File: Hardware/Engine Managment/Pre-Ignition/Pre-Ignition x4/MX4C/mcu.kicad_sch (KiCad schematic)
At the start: 4 parts, among them J8 Reset Control

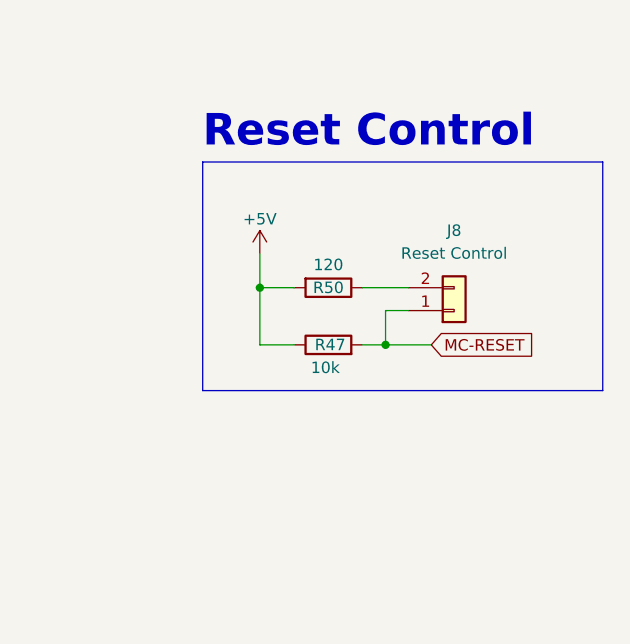
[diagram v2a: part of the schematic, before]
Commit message: minor update
Copper Pour and clearances updated.
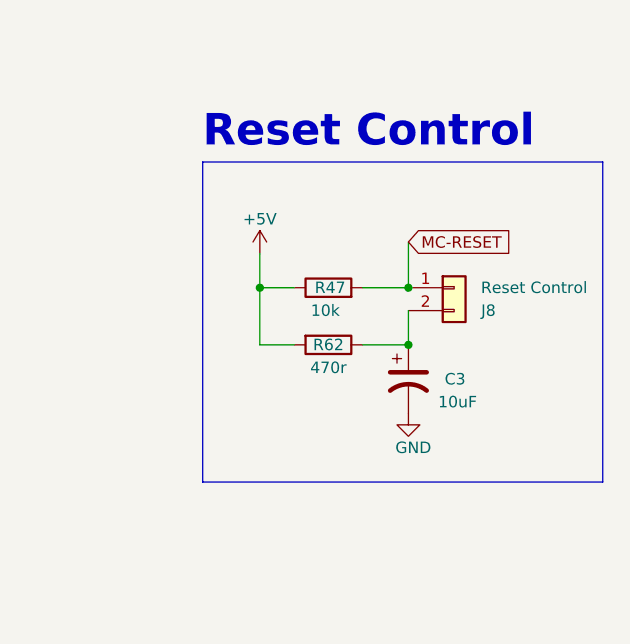
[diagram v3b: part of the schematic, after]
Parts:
- removed R50: 120, Resistor_SMD:R_0402_1005Metric, symbol Device:R
- added C3: 10uF, Capacitor_Tantalum_SMD:CP_EIA-3216-18_Kemet-A, symbol Device:C_Polarized_US
- added R62: 470r, Resistor_SMD:R_0402_1005Metric, symbol Device:R
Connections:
- net +5V: now also R62.2
- net GND: now also C3.2
- net at J8.2 (Pin_2): now also C3.1, R62.1
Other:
- moved on the sheet: R47
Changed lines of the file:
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@@
   (title_block
     (title "Pre-Ignition X4")
-    (date "2023-06-15")
+    (date "2023-10-24")
     (rev "C")
     (company "DetonationEMS")
@@
   (junction (at 57.15 128.27) (diameter 0) (color 0 0 0 0)
   )
+  (junction (at 190.5 115.57) (diameter 0) (color 0 0 0 0)
+  )
   (junction (at 173.99 109.22) (diameter 0) (color 0 0 0 0)
   )
   (junction (at 57.15 133.35) (diameter 0) (color 0 0 0 0)
   )
-  (junction (at 187.96 115.57) (diameter 0) (color 0 0 0 0)
+  (junction (at 190.5 109.22) (diameter 0) (color 0 0 0 0)
   )
   (wire (pts (xy 40.64 146.05) (xy 57.15 146.05))
@@
     (stroke (width 0) (type default))
   )
-  (wire (pts (xy 187.96 111.76) (xy 187.96 115.57))
+  (wire (pts (xy 190.5 111.76) (xy 190.5 115.57))
     (stroke (width 0) (type default))
   )
@@
     (stroke (width 0) (type default))
   )
-  (wire (pts (xy 187.96 115.57) (xy 193.04 115.57))
+  (wire (pts (xy 190.5 104.14) (xy 190.5 109.22))
     (stroke (width 0) (type default))
   )
@@
     (stroke (width 0) (type default))
   )
-  (polyline (pts (xy 167.64 120.65) (xy 212.09 120.65))
+  (polyline (pts (xy 167.64 130.81) (xy 212.09 130.81))
     (stroke (width 0) (type default))
   )
@@
     (stroke (width 0) (type default))
   )
+  (wire (pts (xy 185.42 115.57) (xy 190.5 115.57))
+    (stroke (width 0) (type default))
+  )
   (wire (pts (xy 57.15 128.27) (xy 57.15 130.81))
     (stroke (width 0) (type default))
@@
     (stroke (width 0) (type default))
   )
-  (polyline (pts (xy 212.09 120.65) (xy 212.09 95.25))
+  (polyline (pts (xy 212.09 130.81) (xy 212.09 95.25))
     (stroke (width 0) (type default))
   )
@@
     (stroke (width 0) (type default))
   )
-  (wire (pts (xy 190.5 111.76) (xy 187.96 111.76))
-    (stroke (width 0) (type default))
-  )
   (wire (pts (xy 45.72 140.97) (xy 64.77 140.97))
     (stroke (width 0) (type default))
   )
-  (polyline (pts (xy 167.64 95.25) (xy 167.64 120.65))
+  (polyline (pts (xy 167.64 95.25) (xy 167.64 130.81))
     (stroke (width 0) (type default))
   )
@@
   )
   (wire (pts (xy 60.96 100.33) (xy 64.77 100.33))
-    (stroke (width 0) (type default))
-  )
-  (wire (pts (xy 185.42 115.57) (xy 187.96 115.57))
     (stroke (width 0) (type default))
   )
@@
     )
   )
-  (global_label "MC-RESET" (shape input) (at 193.04 115.57 0) (fields_autoplaced)
-    (effects (font (size 1.27 1.27)) (justify left))
-    (property "Intersheetrefs" "${INTERSHEET_REFS}" (at 101.6 -19.05 0)
+  (global_label "MC-RESET" (shape input) (at 190.5 104.14 0) (fields_autoplaced)
+    (effects (font (size 1.27 1.27)) (justify left))
+    (property "Intersheetrefs" "${INTERSHEET_REFS}" (at 99.06 -30.48 0)
       (effects (font (size 1.27 1.27)) hide)
     )
@@
     )
   )
-  (symbol (lib_id "Device:R") (at 181.61 115.57 90) (unit 1)
+  (symbol (lib_id "Device:R") (at 181.61 109.22 90) (unit 1)
     (in_bom yes) (on_board yes) (dnp no)
-    (property "Reference" "R47" (at 183.515 115.57 90)
+    (property "Reference" "R47" (at 183.515 109.22 90)
       (effects (font (size 1.27 1.27)) (justify left))
     )
-    (property "Value" "10k" (at 182.88 118.11 90)
+    (property "Value" "10k" (at 182.88 111.76 90)
       (effects (font (size 1.27 1.27)) (justify left))
     )
-    (property "Footprint" "Resistor_SMD:R_0603_1608Metric" (at 181.61 117.348 90)
-      (effects (font (size 1.27 1.27)) hide)
-    )
-    (property "Datasheet" "~" (at 181.61 115.57 0)
-      (effects (font (size 1.27 1.27)) hide)
-    )
-    (property "LCSC" "C25804" (at 181.61 115.57 0)
+    (property "Footprint" "Resistor_SMD:R_0603_1608Metric" (at 181.61 110.998 90)
+      (effects (font (size 1.27 1.27)) hide)
+    )
+    (property "Datasheet" "~" (at 181.61 109.22 0)
+      (effects (font (size 1.27 1.27)) hide)
+    )
+    (property "LCSC" "C25804" (at 181.61 109.22 0)
       (effects (font (size 1.27 1.27)) hide)
     )
@@
     )
   )
+  (symbol (lib_id "Device:R") (at 181.61 115.57 270) (unit 1)
+    (in_bom yes) (on_board yes) (dnp no)
+    (property "Reference" "R62" (at 181.61 115.57 90)
+      (effects (font (size 1.27 1.27)))
+    )
+    (property "Value" "470r" (at 181.61 118.11 90)
+      (effects (font (size 1.27 1.27)))
+    )
+    (property "Footprint" "Resistor_SMD:R_0402_1005Metric" (at 181.61 113.792 90)
+      (effects (font (size 1.27 1.27)) hide)
+    )
+    (property "Datasheet" "~" (at 181.61 115.57 0)
+      (effects (font (size 1.27 1.27)) hide)
+    )
+    (property "LCSC" "C25117" (at 181.61 115.57 0)
+      (effects (font (size 1.27 1.27)) hide)
+    )
+    (pin "1")
+    (pin "2")
+    (instances
+      (project "Pre_Ignition"
+        (path "/929a9b03-e99e-4b88-8e16-759f8c6b59a5/00000000-0000-0000-0000-000060e7aa2a"
+          (reference "R62") (unit 1)
+        )
+        (path "/929a9b03-e99e-4b88-8e16-759f8c6b59a5/651424fd-2282-475b-821e-32691fc06f26"
+          (reference "R62") (unit 1)
+        )
+      )
+    )
+  )
   (symbol (lib_id "power:GND") (at 53.34 128.27 0) (unit 1)
     (in_bom yes) (on_board yes) (dnp no)
@@
     )
   )
-  (symbol (lib_id "Connector_Generic:Conn_01x02") (at 195.58 111.76 0) (mirror x) (unit 1)
-    (in_bom yes) (on_board yes) (dnp no) (fields_autoplaced)
-    (property "Reference" "J8" (at 195.58 102.87 0)
+  (symbol (lib_id "Connector_Generic:Conn_01x02") (at 195.58 109.22 0) (unit 1)
+    (in_bom yes) (on_board yes) (dnp no)
+    (property "Reference" "J8" (at 199.39 111.76 0)
       (effects (font (size 1.27 1.27)))
     )
-    (property "Value" "Reset Control" (at 195.58 105.41 0)
+    (property "Value" "Reset Control" (at 204.47 109.22 0)
       (effects (font (size 1.27 1.27)))
     )
-    (property "Footprint" "Detonation:1x02-Proto" (at 195.58 111.76 0)
-      (effects (font (size 1.27 1.27)) hide)
-    )
-    (property "Datasheet" "~" (at 195.58 111.76 0)
+    (property "Footprint" "Detonation:1x02-Proto" (at 195.58 109.22 0)
+      (effects (font (size 1.27 1.27)) hide)
+    )
+    (property "Datasheet" "~" (at 195.58 109.22 0)
       (effects (font (size 1.27 1.27)) hide)
     )
@@
     )
   )
-  (symbol (lib_id "Device:R") (at 181.61 109.22 270) (unit 1)
+  (symbol (lib_id "Device:C_Polarized_US") (at 190.5 119.38 0) (unit 1)
     (in_bom yes) (on_board yes) (dnp no)
-    (property "Reference" "R50" (at 181.61 109.22 90)
-      (effects (font (size 1.27 1.27)))
-    )
-    (property "Value" "120" (at 181.61 106.68 90)
-      (effects (font (size 1.27 1.27)))
-    )
-    (property "Footprint" "Resistor_SMD:R_0402_1005Metric" (at 181.61 107.442 90)
-      (effects (font (size 1.27 1.27)) hide)
-    )
-    (property "Datasheet" "~" (at 181.61 109.22 0)
-      (effects (font (size 1.27 1.27)) hide)
-    )
-    (property "LCSC" "C25079" (at 181.61 109.22 0)
+    (property "Reference" "C3" (at 196.85 119.38 0)
+      (effects (font (size 1.27 1.27)) (justify right))
+    )
+    (property "Value" "10uF" (at 198.12 121.92 0)
+      (effects (font (size 1.27 1.27)) (justify right))
+    )
+    (property "Footprint" "Capacitor_Tantalum_SMD:CP_EIA-3216-18_Kemet-A" (at 190.5 119.38 0)
+      (effects (font (size 1.27 1.27)) hide)
+    )
+    (property "Datasheet" "~" (at 190.5 119.38 0)
+      (effects (font (size 1.27 1.27)) hide)
+    )
+    (property "LCSC" "C7171" (at 190.5 119.38 0)
+      (effects (font (size 1.27 1.27)) hide)
+    )
+    (property "Manufacture Part Number" "TAJA106K016RNJ" (at 190.5 119.38 0)
       (effects (font (size 1.27 1.27)) hide)
     )
@@
     (instances
       (project "Pre_Ignition"
+        (path "/4af6cfdf-466c-4a30-a9ae-01184b002ed6/46f448a6-75c3-4ecc-b10a-dcee0521adb1"
+          (reference "C3") (unit 1)
+        )
+      )
+      (project "Pre_Ignition"
+        (path "/929a9b03-e99e-4b88-8e16-759f8c6b59a5/fd679192-a7db-468f-89ad-a9c384ea113f"
+          (reference "C33") (unit 1)
+        )
         (path "/929a9b03-e99e-4b88-8e16-759f8c6b59a5/651424fd-2282-475b-821e-32691fc06f26"
-          (reference "R50") (unit 1)
+          (reference "C31") (unit 1)
         )
       )
@@
         )
       )
+    )
+  )
+  (symbol (lib_id "power:GND") (at 190.5 123.19 0) (unit 1)
+    (in_bom yes) (on_board yes) (dnp no)
+    (property "Reference" "#PWR051" (at 190.5 129.54 0)
+      (effects (font (size 1.27 1.27)) hide)
+    )
+    (property "Value" "GND" (at 193.04 127 0)
+      (effects (font (size 1.27 1.27)) (justify right))
+    )
+    (property "Footprint" "" (at 190.5 123.19 0)
+      (effects (font (size 1.27 1.27)) hide)
+    )
+    (property "Datasheet" "" (at 190.5 123.19 0)
+      (effects (font (size 1.27 1.27)) hide)
+    )
+    (pin "1")
+    (instances
+      (project "Pre_Ignition"
+        (path "/929a9b03-e99e-4b88-8e16-759f8c6b59a5/651424fd-2282-475b-821e-32691fc06f26"
+          (reference "#PWR051") (unit 1)
+        )
+      )

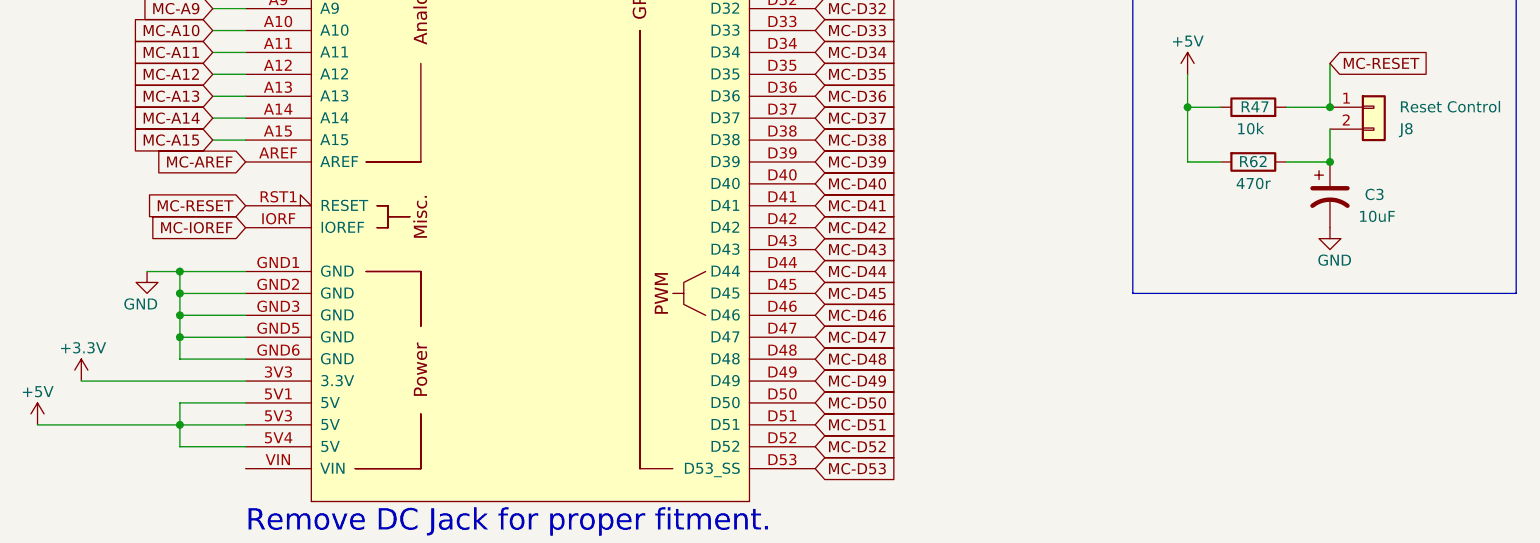
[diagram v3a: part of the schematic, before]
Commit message: schematic exports
kicad version updates, schematic exports
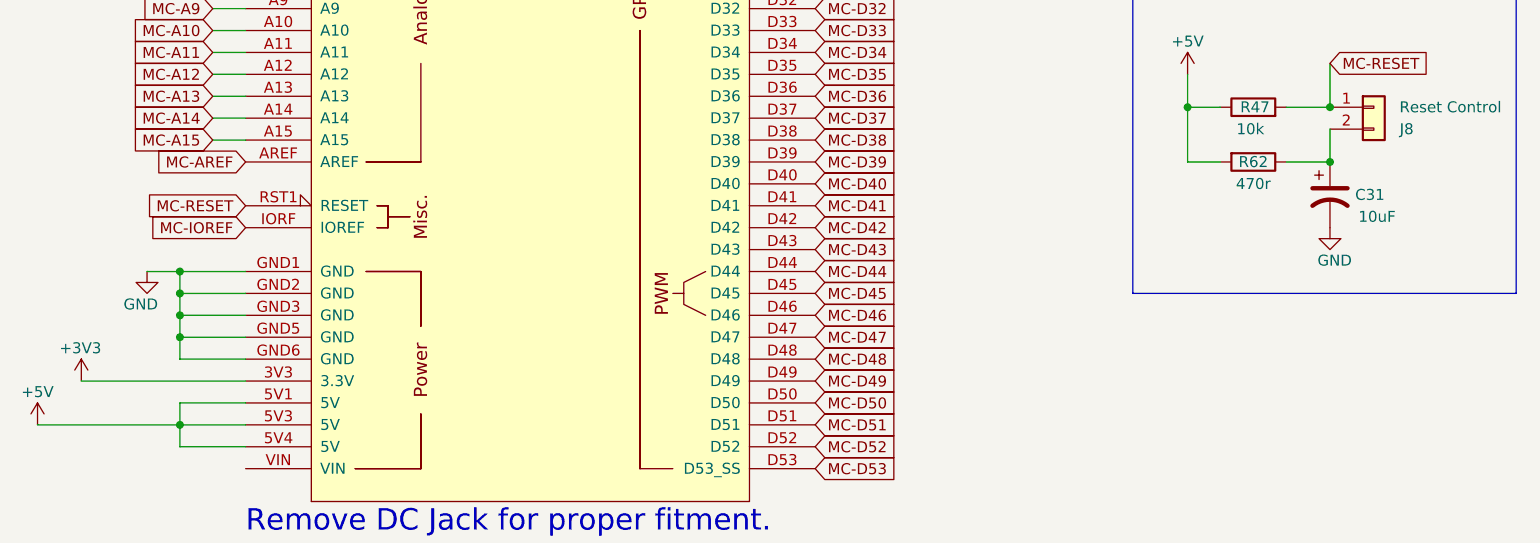
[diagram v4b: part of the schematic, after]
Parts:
- renumbered C3 to C31
